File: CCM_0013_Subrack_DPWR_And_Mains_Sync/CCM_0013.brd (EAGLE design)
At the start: 82.5 x 99.1 mm, 12 parts, among them X15 MAB64

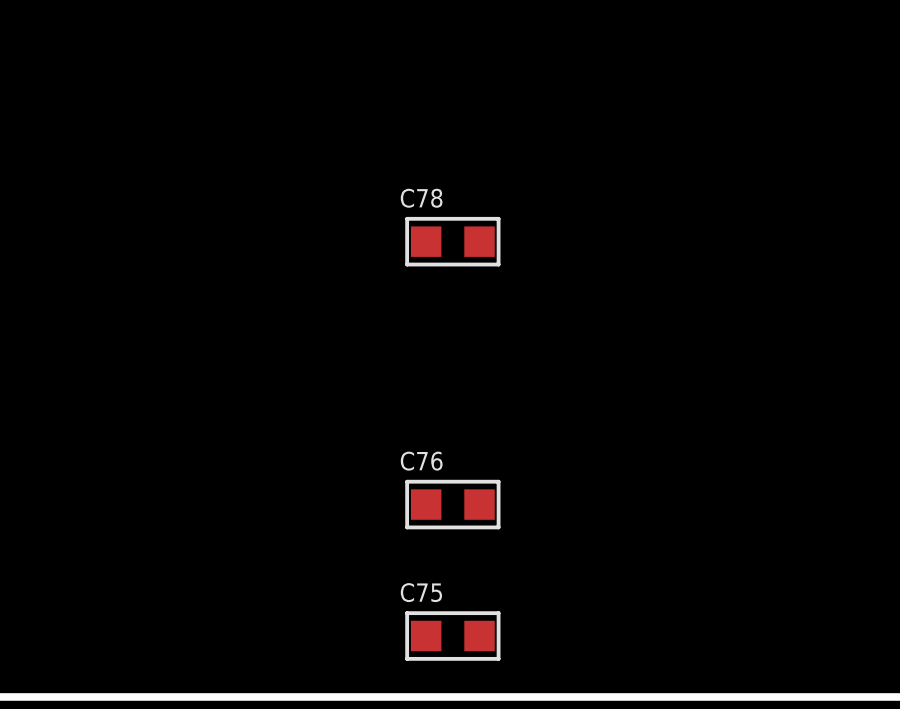
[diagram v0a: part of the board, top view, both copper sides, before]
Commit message: Shutter driver added.
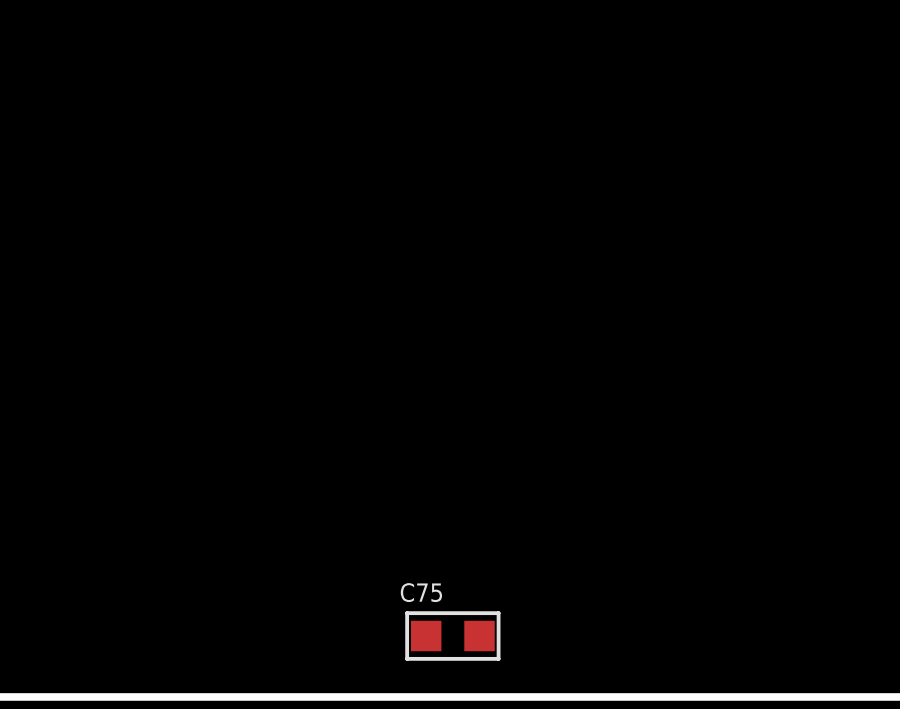
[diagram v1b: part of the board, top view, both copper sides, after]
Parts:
- removed C76: 0.1u, acrooptics:0603
- removed C78: 4.7u, acrooptics:0603
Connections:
- removed net 3.3V: C76.1, C78.1
- net GND: no longer C76.2, C78.2
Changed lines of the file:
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@@
 <?xml version="1.0" encoding="utf-8"?>
 <!DOCTYPE eagle SYSTEM "eagle.dtd">
-<eagle version="8.6.0">
+<eagle version="9.0.1">
 <drawing>
 <settings>
@@
 <attribute name="VALUE" x="62.611" y="99.314" size="0.6096" layer="27" font="vector" ratio="20"/>
 </element>
-<element name="C76" library="acrooptics" package="0603" value="0.1u" x="64.262" y="105.4735" smashed="yes">
-<attribute name="NAME" x="62.484" y="106.6165" size="0.6096" layer="25" font="vector" ratio="20"/>
-<attribute name="VALUE" x="62.611" y="103.6955" size="0.6096" layer="27" font="vector" ratio="20"/>
-</element>
-<element name="C78" library="acrooptics" package="0603" value="4.7u" x="64.262" y="114.2365" smashed="yes">
-<attribute name="NAME" x="62.484" y="115.3795" size="0.6096" layer="25" font="vector" ratio="20"/>
-<attribute name="VALUE" x="62.611" y="112.4585" size="0.6096" layer="27" font="vector" ratio="20"/>
-</element>
 <element name="D9" library="diode" library_urn="urn:adsk.eagle:library:210" package="SOT23" package3d_urn="urn:adsk.eagle:package:43389/2" value="BAT54S" x="-53.5305" y="95.123" smashed="yes">
 <attribute name="NAME" x="-55.4355" y="97.028" size="1.27" layer="25"/>
@@
 <vertex x="81.28" y="1.27"/>
 </polygon>
-<contactref element="C76" pad="2"/>
-<contactref element="C78" pad="2"/>
 <contactref element="D9" pad="1"/>
 <contactref element="D9" pad="2"/>
@@
 <contactref element="X15" pad="A3"/>
 <contactref element="X15" pad="A26"/>
-<wire x1="-52.5805" y1="94.023" x2="-54.4805" y2="94.023" width="0" layer="19" extent="1-1"/>
-<wire x1="74.6125" y1="86.36" x2="-52.5805" y2="94.023" width="0" layer="19" extent="1-1"/>
+<wire x1="74.6125" y1="86.36" x2="77.1525" y2="86.36" width="0" layer="19" extent="1-1"/>
+<wire x1="77.1525" y1="83.82" x2="77.1525" y2="86.36" width="0" layer="19" extent="1-1"/>
 <wire x1="74.6125" y1="83.82" x2="74.6125" y2="86.36" width="0" layer="19" extent="1-1"/>
-<wire x1="77.1525" y1="83.82" x2="74.6125" y2="83.82" width="0" layer="19" extent="1-1"/>
-<wire x1="77.1525" y1="86.36" x2="74.6125" y2="86.36" width="0" layer="19" extent="1-1"/>
 <wire x1="74.6125" y1="43.18" x2="74.6125" y2="83.82" width="0" layer="19" extent="1-1"/>
 <wire x1="74.6125" y1="40.64" x2="74.6125" y2="43.18" width="0" layer="19" extent="1-1"/>
@@
 <wire x1="74.6125" y1="25.4" x2="74.6125" y2="27.94" width="0" layer="19" extent="1-1"/>
 <wire x1="77.1525" y1="25.4" x2="74.6125" y2="25.4" width="0" layer="19" extent="1-1"/>
-<wire x1="65.151" y1="105.4735" x2="-54.4805" y2="94.023" width="0" layer="19" extent="1-1"/>
-<wire x1="65.151" y1="114.2365" x2="65.151" y2="105.4735" width="0" layer="19" extent="1-1"/>
+<wire x1="-52.5805" y1="94.023" x2="74.6125" y2="86.36" width="0" layer="19" extent="1-1"/>
+<wire x1="-54.4805" y1="94.023" x2="-52.5805" y2="94.023" width="0" layer="19" extent="1-1"/>
 </signal>
 <signal name="AGND">
@@
 <wire x1="-29.972" y1="176.8475" x2="-31.75" y2="172.466" width="0" layer="19" extent="1-1"/>
 </signal>
-<signal name="3.3V">
-<contactref element="C78" pad="1"/>
-<contactref element="C76" pad="1"/>
-<wire x1="63.373" y1="114.2365" x2="63.373" y2="105.4735" width="0" layer="19" extent="1-1"/>
-</signal>
 <signal name="+5V">
 <contactref element="C74" pad="1"/>
@@
 </signal>
 </signals>
-<errors>
-</errors>
 </board>
 </drawing>
